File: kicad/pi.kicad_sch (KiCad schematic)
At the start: 13 parts, among them J1 Conn_02x20_Odd_Even, M1 Fan_4pin, U13 TMP1075

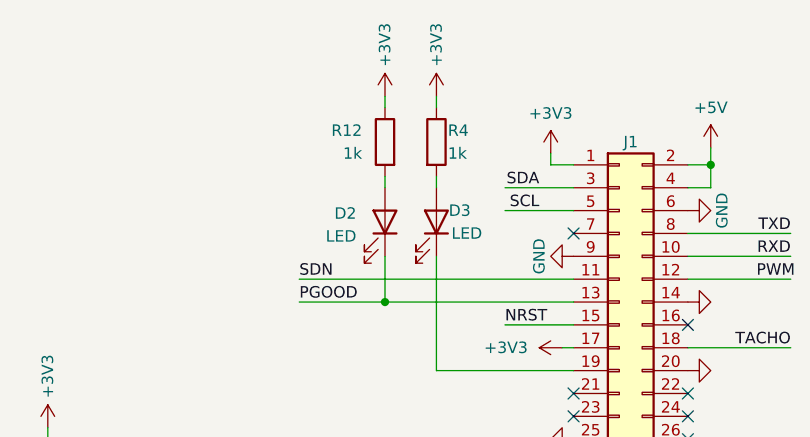
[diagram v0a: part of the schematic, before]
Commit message: added solderjumper to enable the buck without Pi, changed LED values to 560R
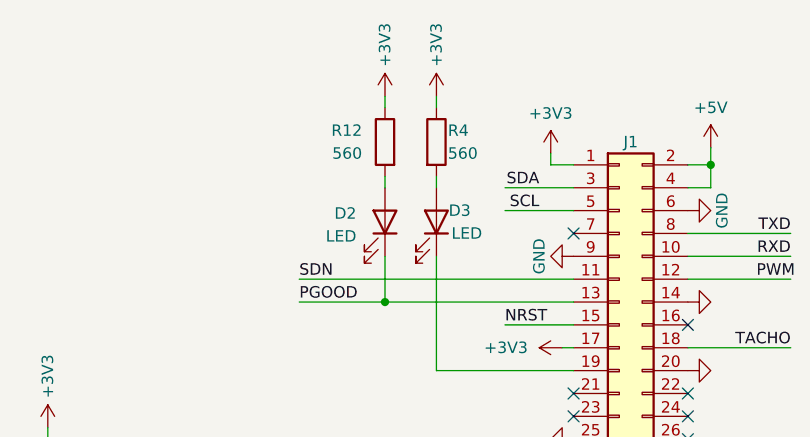
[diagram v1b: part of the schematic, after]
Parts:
- R12, R4: value 1k -> 560
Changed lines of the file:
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@@
       (effects (font (size 1.27 1.27)) (justify left))
     )
-    (property "Value" "1k" (at 165.1 69.85 0)
+    (property "Value" "560" (at 165.1 69.85 0)
       (effects (font (size 1.27 1.27)) (justify left))
     )
@@
       (effects (font (size 1.27 1.27)) (justify left))
     )
-    (property "Value" "1k" (at 155.575 69.85 0)
-      (effects (font (size 1.27 1.27)) (justify left))
-    )
+    (property "Value" "560" (at 155.575 69.85 0)
+      (effects (font (size 1.27 1.27)) (justify left))
+    )

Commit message: initial commit before replacing power supply
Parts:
- removed J1: Conn_02x20_Odd_Even, Connector_PinHeader_2.54mm:PinHeader_2x20_P2.54mm_Vertical, symbol pearldiver-rescue:Conn_02x20_Odd_Even-pearldiver-rescue
- removed JP1: SolderJumper_3_Open, Jumper:SolderJumper-3_P1.3mm_Open_RoundedPad1.0x1.5mm, symbol Jumper:SolderJumper_3_Open
- added C5, C6, C9: 100n, Capacitor_SMD:C_0805_2012Metric, symbol vfd1-rescue:C
- added J5: SWD, myfootprints:PinHeader_IDC_2x05_P1.27mm_Vertical_SMD, symbol dwc-hat-rescue:Conn_02x05_Odd_Even-Connector_Generic
- added P2: MYUSB_B, Connector_USB:USB_Micro-B_Amphenol_10103594-0001LF_Horizontal, symbol clock-rescue:MYUSB_B
- added R23: 100k, Resistor_SMD:R_0805_2012Metric, symbol Device:R
- added R27, R28: 10k, Resistor_SMD:R_0805_2012Metric, symbol dwc-hat-rescue:R-Device
- added R29: 1.5k, Resistor_SMD:R_0805_2012Metric, symbol Device:R
- added R36, R37: 22, Resistor_SMD:R_0805_2012Metric, symbol clock-rescue:R
- added U3: STM32L052K6Tx, Package_QFP:LQFP-32_7x7mm_P0.8mm, symbol MCU_ST_STM32L0:STM32L052K6Tx
- renumbered D2 to D5, D3 to D6, M1 to M2, R15 to R26, R14 to R27, R11 to R28, R10 to R29, R12 to R30, R4 to R31
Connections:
- net +12V: now also M2.2 (+)
- net +3V3: now also C5.1, C6.1, C9.1, R27.2, R29.1, U3.1 (VDD), U3.17 (VDD), U3.5 (VDDA)
- net +5V: now also P2.1 (VCC)
- net BUCK_POWER_GOOD: no longer D5.1 (K)
- net GND: now also C5.2, C6.2, C9.2, J5.3 (Pin_3), J5.4 (Pin_4), P2.5 (GND), P2.6 (shield), R23.1, R28.1, U3.16 (VSS), U3.32 (VSS)
- net LED1: now reaches D6.1 (K)
- net LED1: now also U3.12 (PA6)
- net ALERT renamed TMP_ALARM
- net TMP_ALARM: now also U3.28 (PB5)
- net PWM renamed FAN_PWM
- net FAN_PWM: now also U3.6 (PA0)
- net SCL renamed TMP_SCL
- net TMP_SCL: now also U3.29 (PB6)
- net SDA renamed TMP_SDA
- net TMP_SDA: now also U3.30 (PB7)
- net TACHO renamed FAN_TACHO
- net FAN_TACHO: now also U3.7 (PA1)
- new net: P2.2 (D-), R36.2
- new net: P2.3 (D+), R37.2
- new net: R23.2, U3.31 (BOOT0)
- new net 1V2_PGOOD: R29.2, U3.15 (PB1)
- new net 1V2_RUN: U3.14 (PB0)
- new net ARM_NRST: J5.1 (Pin_1), U3.4 (NRST)
- new net ARM_SWCLK: J5.6 (Pin_6), R28.2, U3.24 (PA14)
- new net ARM_SWDIO: J5.2 (Pin_2), R27.1, U3.23 (PA13)
- new net LED2: D5.1 (K), U3.13 (PA7)
- new net RX: U3.19 (PA9)
- new net TX: U3.20 (PA10)
- new net USB_D+: R37.1, U3.22 (PA12)
- new net USB_D-: R36.1, U3.21 (PA11)
- no-connect marks 17 -> 6
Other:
- note removed: "Raspberry Pi GPIO"
- moved on the sheet: C23, D5, D6, M2, R26, R27, R28, R29, R30, R31, U13

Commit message: updated gerber, bom
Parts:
- added Q1: BSS138, Package_TO_SOT_SMD:SOT-23, symbol Transistor_FET:BSS138
- C23: PARTNO 0402X104K100CT -> (none)
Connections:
- net GND: now also Q1.2 (S)
- net RESET: now reaches U3.18 (PA8)
- net ARM_NRST renamed NRST
- net ARM_SWCLK renamed SWCLK
- net ARM_SWDIO renamed SWDIO
- net FAN_PWM: no longer names the net of M2.4 (PWM)
- net FAN_PWM: now also Q1.3 (D); no longer U3.6 (PA0)
- net FAN_TACHO renamed TACHO
- net RX renamed TXD
- net TMP_ALARM renamed ALERT
- net TMP_SCL renamed SCL
- net TMP_SDA renamed SDA
- net TX renamed RXD
- new net PWM: Q1.1 (G), U3.6 (PA0)
- no-connect marks 6 -> 15
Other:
- moved on the sheet: C23, C5, C6, C9, D5, D6, J5, M2, P2, R23, R26, R27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

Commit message: v0.02
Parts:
- removed C5: 100n, Capacitor_SMD:C_0805_2012Metric, symbol vfd1-rescue:C
- removed P2: MYUSB_B, Connector_USB:USB_Micro-B_Amphenol_10103594-0001LF_Horizontal, symbol clock-rescue:MYUSB_B
- removed Q1: BSS138, Package_TO_SOT_SMD:SOT-23, symbol Transistor_FET:BSS138
- removed U3: STM32L052K6Tx, Package_QFP:LQFP-32_7x7mm_P0.8mm, symbol MCU_ST_STM32L0:STM32L052K6Tx
- added C23 (x6): 100n, Capacitor_SMD:C_0805_2012Metric, symbol Device:C
- added C55: 22µ/25V, Capacitor_SMD:C_1210_3225Metric, symbol Device:C
- added C9 (x2): 100n, Capacitor_SMD:C_0805_2012Metric, symbol vfd1-rescue:C
- added J4, J5: Conn_01x02, Connector_PinHeader_2.54mm:PinHeader_1x02_P2.54mm_Vertical, symbol Connector_Generic:Conn_01x02
- added J6: USB_C_Receptacle_USB2.0, Connector_USB:USB_C_Receptacle_GCT_USB4105-xx-A_16P_TopMnt_Horizontal, symbol Connector:USB_C_Receptacle_USB2.0
- added M2: Fan_4pin, Connector:FanPinHeader_1x04_P2.54mm_Vertical, symbol Motor:Fan_4pin
- added R28: 2.7k, Resistor_SMD:R_0805_2012Metric, symbol Device:R
- added R30, R31: 560, Resistor_SMD:R_0805_2012Metric, symbol Device:R
- added R36 (x2): 5.1k, Resistor_SMD:R_0805_2012Metric, symbol clock-rescue:R
- added U13: TMP1075, myfootprints:TMP1075-DRL, symbol mylib7:TMP1075-DRL-SOT563
- added U35: STM32L151C8TxA, Package_QFP:LQFP-48_7x7mm_P0.5mm, symbol MCU_ST_STM32L1:STM32L151C8TxA
- added U37, U39: TXU0101, Package_TO_SOT_SMD:SOT-363_SC-70-6, symbol mylib7:TXU0101DCK
- added X1: 8MHz, Oscillator:Oscillator_SMD_EuroQuartz_XO32-4Pin_3.2x2.5mm, symbol Oscillator:XO32
- R28: value 2k2 -> 2.7k
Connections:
- net +12V: now also C55.1, M2.2 (+)
- net +3V3: now also C23.1, C23.1, C23.1, C23.1, C9.1, C9.1, R28.1, R30.1, R31.1, U13.4 (A0), U13.5 (V+), U35.1 (VLCD), U35.24 (VDD), U35.36 (VDD), U35.48 (VDD), U35.9 (VDDA), U37.1 (VCCA), U39.1 (VCCA), X1.1 (EN), X1.4 (V+)
- net +5V: now also C23.1, C23.1, U37.5 (OE), U37.6 (VCCB), U39.5 (OE), U39.6 (VCCB)
- net 1V2_PGOOD: now also U35.13 (PA3)
- net 1V2_RUN: now also U35.12 (PA2)
- net GND: now also C23.2, C23.2, C23.2, C23.2, C23.2, C23.2, C55.2, C9.2, C9.2, J6.A1 (GND), J6.A12 (GND), J6.B1 (GND), J6.B12 (GND), J6.S1 (SHIELD), M2.1 (-), R36.1, R36.1, U13.2 (GND), U35.23 (VSS), U35.35 (VSS), U35.47 (VSS), U35.8 (VSSA), U37.2 (GND), U39.2 (GND), X1.2 (GND)
- net LED1: now also U35.14 (PA4)
- net LED2: now also U35.15 (PA5)
- net NRST: now also U35.7 (NRST)
- net RESET: now also U35.26 (PB13)
- net RXD: now also U35.31 (PA10)
- net SWCLK: now also U35.37 (PA14)
- net SWDIO: now also U35.34 (PA13)
- net TXD: now also U35.30 (PA9)
- net USB_D+: now also U35.33 (PA12)
- net USB_D-: now also U35.32 (PA11)
- net at R36.2: now also J6.A7 (D-), J6.B7 (D-)
- net at R37.2: now also J6.A6 (D+), J6.B6 (D+)
- net at M2.4 (PWM): now also U39.4 (BY)
- net at R23.2: now also U35.44 (BOOT0)
- net ALERT renamed ALERT2
- net ALERT2: now also U13.3 (ALERT), U35.25 (PB12)
- net SCL renamed SCL2
- net SCL2: now also U13.1 (SCL), U35.21 (PB10)
- net SDA renamed SDA2
- net SDA2: now also U13.6 (SDA), U35.22 (PB11)
- net TACHO renamed TACHO1
- net TACHO1: now also U35.16 (PA6)
- new net: M2.4 (PWM), U37.4 (BY)
- new net: J5.1 (Pin_1), R31.2
- new net: J6.A5 (CC1), R36.2
- new net: J4.1 (Pin_1), R30.2
- new net: U35.5 (PH0), X1.3 (OUT)
- new net: J6.B5 (CC2), R36.2
- new net: J6.A4 (VBUS), J6.A9 (VBUS), J6.B4 (VBUS), J6.B9 (VBUS)
- new net LED3: J4.2 (Pin_2), U35.38 (PA15)
- new net LED4: J5.2 (Pin_2), U35.46 (PB9)
- new net PWM1: U35.10 (PA0), U39.3 (A)
- new net PWM2: U35.11 (PA1), U37.3 (A)
- new net TACHO2: M2.3 (Tacho), R28.2, U35.42 (PB6)
- no-connect marks 15 -> 24
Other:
- moved on the sheet: C23, C6, C9, D5, D6, J5, M2, R23, R26, R27, R28, R29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
